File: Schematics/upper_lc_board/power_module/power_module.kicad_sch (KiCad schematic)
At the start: 25 parts, among them U13 ID_LM66100DCKR, U14 ID_LM66100DCKR, U3 AMS1117-3.3

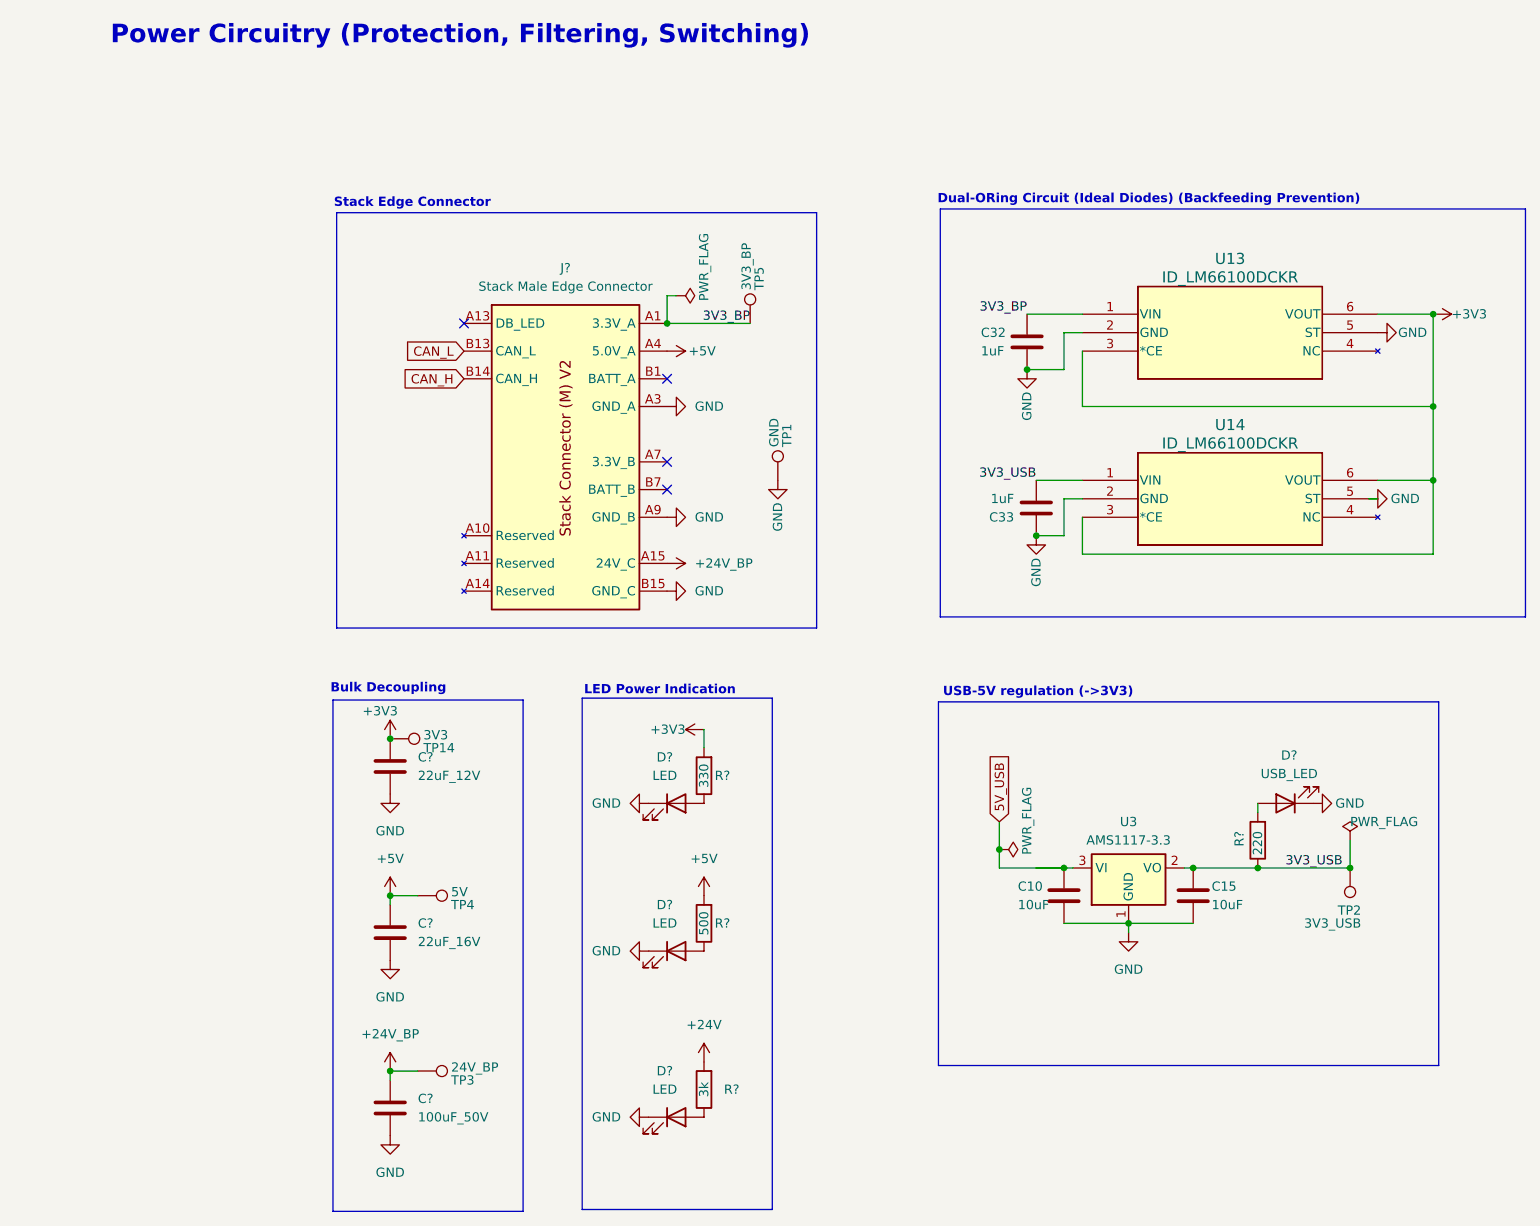
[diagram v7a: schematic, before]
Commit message: switching to primarily 0603 footprints and started adding LSCS numbers
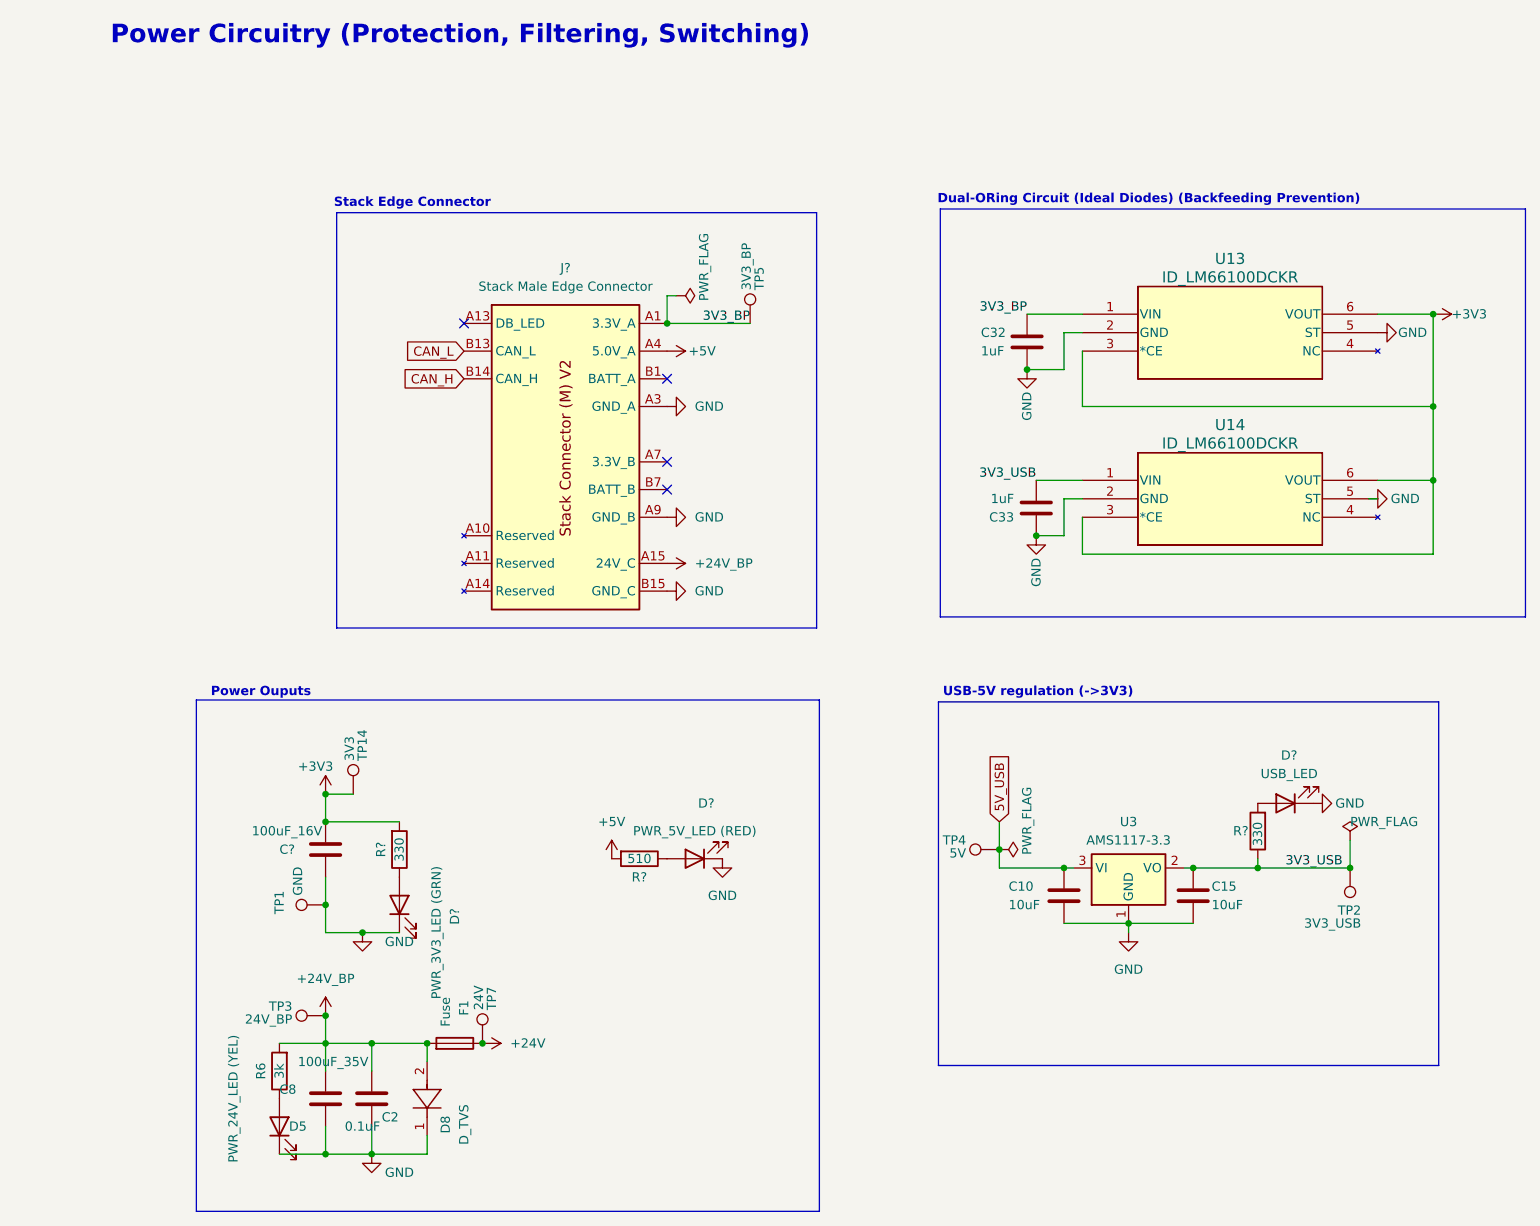
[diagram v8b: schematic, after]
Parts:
- removed C?: 22uF_16V, Capacitor_SMD:CP_Elec_4x5.4, symbol Device:C
- removed C?: 100uF_50V, Capacitor_SMD:CP_Elec_8x10.5, symbol Device:C
- removed D?: LED, LED_SMD:LED_0805_2012Metric, symbol Device:LED
- removed R?: 3k, Resistor_SMD:R_0402_1005Metric, symbol Device:R
- added C2: 0.1uF, Capacitor_SMD:C_0603_1608Metric, symbol Device:C
- added C8: 100uF_35V, Capacitor_SMD:CP_Elec_6.3x5.9, symbol Device:C
- added D5: PWR_24V_LED (YEL), LED_SMD:LED_0805_2012Metric, symbol Device:LED
- added D8: D_TVS, SMA6L30A:SMASeries_LTF-L, symbol SMA6L30A:SMA6L30A
- added F1: Fuse, 0679L0250-05:FUSC6125X279N, symbol Device:Fuse
- added R6: 3k, Resistor_SMD:R_0402_1005Metric, symbol Device:R
- added TP7: 24V, TestPoint:TestPoint_Pad_D1.0mm, symbol Connector:TestPoint
- C10, C15: JLCPCB C96446 -> (none); LCSC (none) -> C96446
- C32, C33: LCSC (none) -> C15849
- C?: value 22uF_12V -> 100uF_16V; footprint Capacitor_SMD:CP_Elec_4x5.4 -> Capacitor_SMD:CP_Elec_6.3x5.9; LCSC (none) -> 732-8419-1-ND
- D?: value LED -> PWR_5V_LED (RED)
- D?: value LED -> PWR_3V3_LED (GRN)
- R?: value 220 -> 330; footprint Resistor_SMD:R_0402_1005Metric -> Resistor_SMD:R_0603_1608Metric; LCSC (none) -> C23138
- R?: value 500 -> 510; footprint Resistor_SMD:R_0402_1005Metric -> Resistor_SMD:R_0603_1608Metric; LCSC (none) -> C23193
- R?: footprint Resistor_SMD:R_0402_1005Metric -> Resistor_SMD:R_0603_1608Metric; LCSC (none) -> C23138
- U3: JLCPCB C6186 -> (none); LSCS (none) -> C6186
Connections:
- net +24V: now also F1.1, TP7.1
- net +24V_BP: now also C2.1, C8.1, D8.2, F1.2, R6.2
- net +5V: no longer TP4.1
- net 5V_USB: now also TP4.1
- net GND: now also C2.2, C8.2, D5.1 (K), D8.1
- new net: D5.2 (A), R6.1
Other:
- note added: "Power Ouputs"
- note removed: "Bulk Decoupling"
- note removed: "LED Power Indication"
- moved on the sheet: C?, D?, R?, TP1, TP14, TP3, TP4
